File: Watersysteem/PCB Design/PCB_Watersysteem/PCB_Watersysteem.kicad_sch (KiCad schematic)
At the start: 67 parts, among them J1 Height Water, J10 ReferentieProbe, J11 Endstop Lade0, J13 LED Water Level, J14 LED Nutrient Level, J15 Voedingsstoffen 1, J18 Backup GPIO, J19 Voedingsstoffen 2, J2 Height Nutrients, J21 Voedingsstoffen 3, J3 Height Mixer, J4 TestPins, J5 12V ingang, J7 TTL Connector, J8 Endstop UV, J9 Endstop Lade1, SW1 EN, SW2 BOOT, U1 MP1584_Module, U2 ESP32-WROOM-32D, U3 ADS1115IDGS, U4 AMS1117-3.3, U5 MCP23017_SO

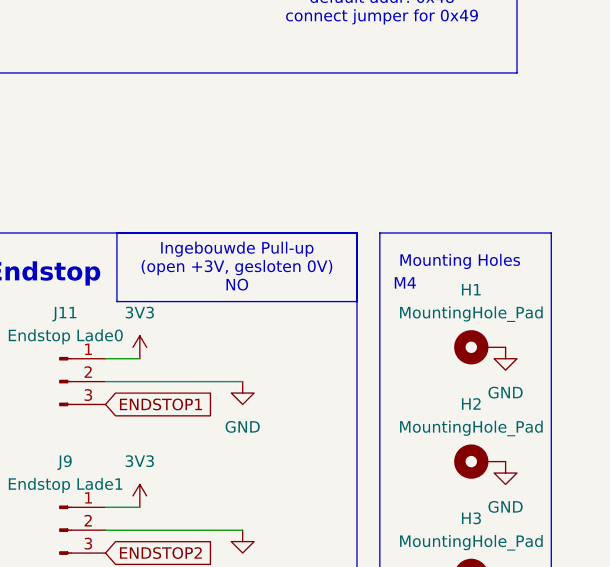
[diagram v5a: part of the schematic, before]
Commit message: Update PCB
M4 -> M3 in Schema
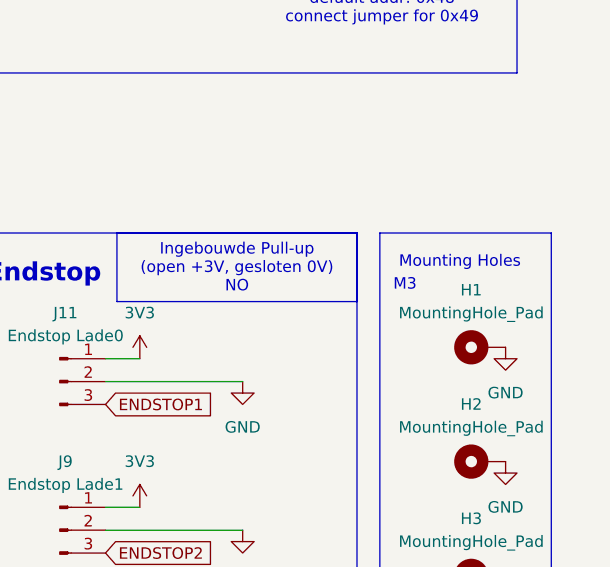
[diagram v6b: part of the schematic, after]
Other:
- note added: "M3"
- note removed: "M4"
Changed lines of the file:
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@@
 		)
 	)
-	(text "M4"
+	(text "M3"
 		(exclude_from_sim no)
 		(at 268.224 112.522 0)

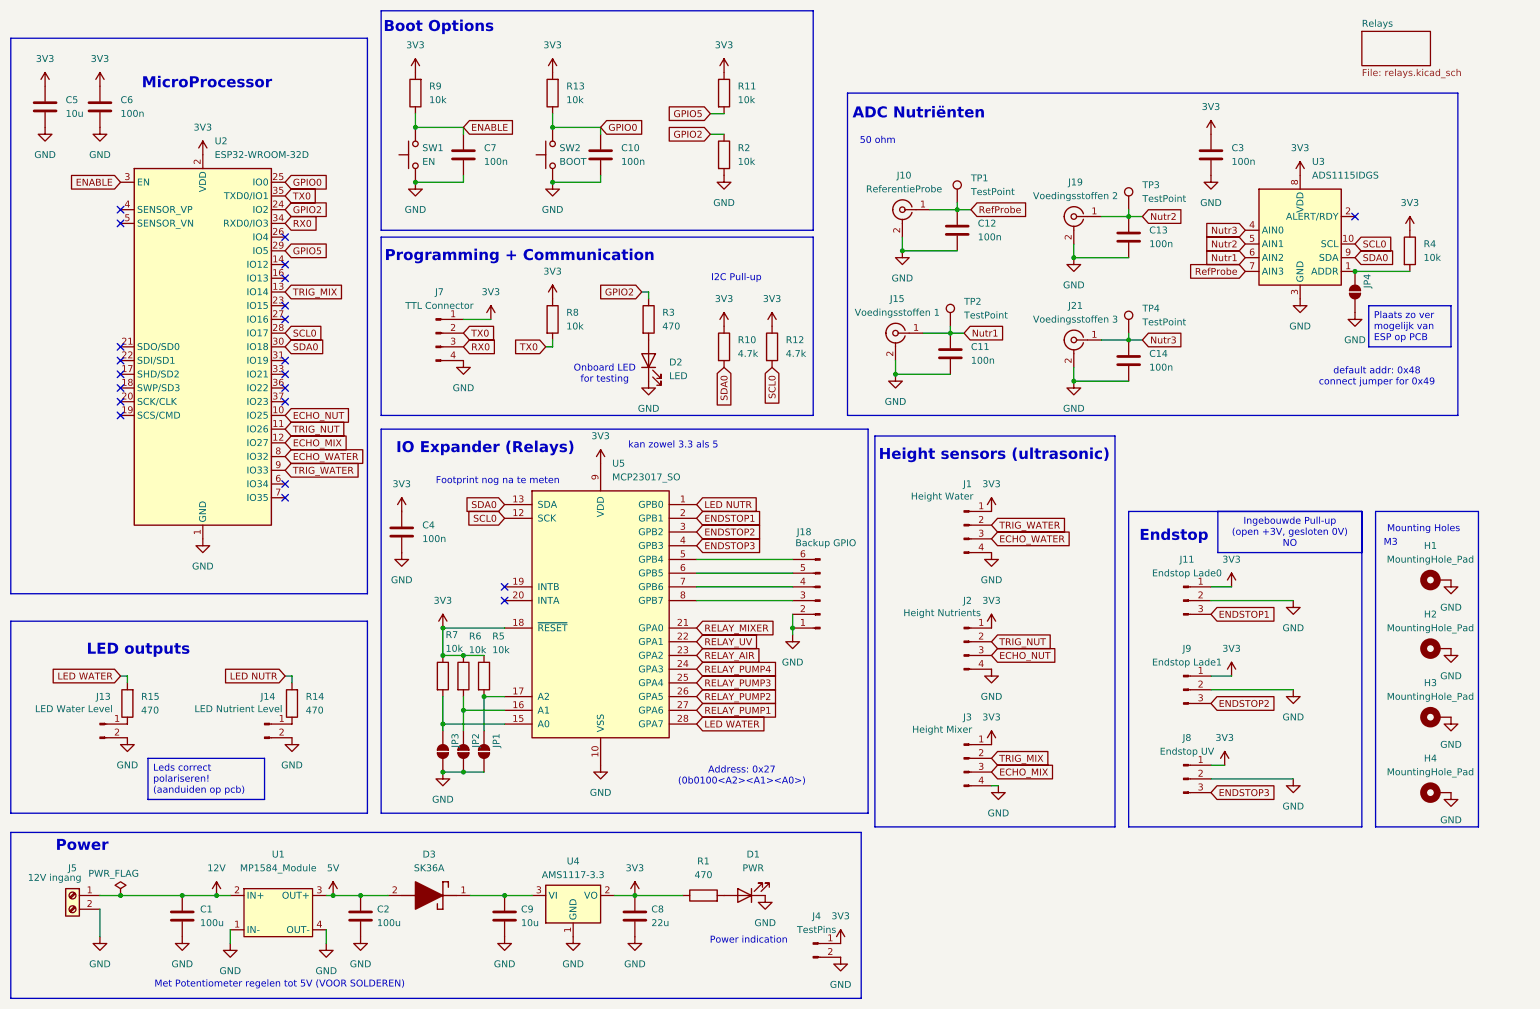
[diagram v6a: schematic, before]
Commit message: Weerstandjes gewijzigd voor status LEDs
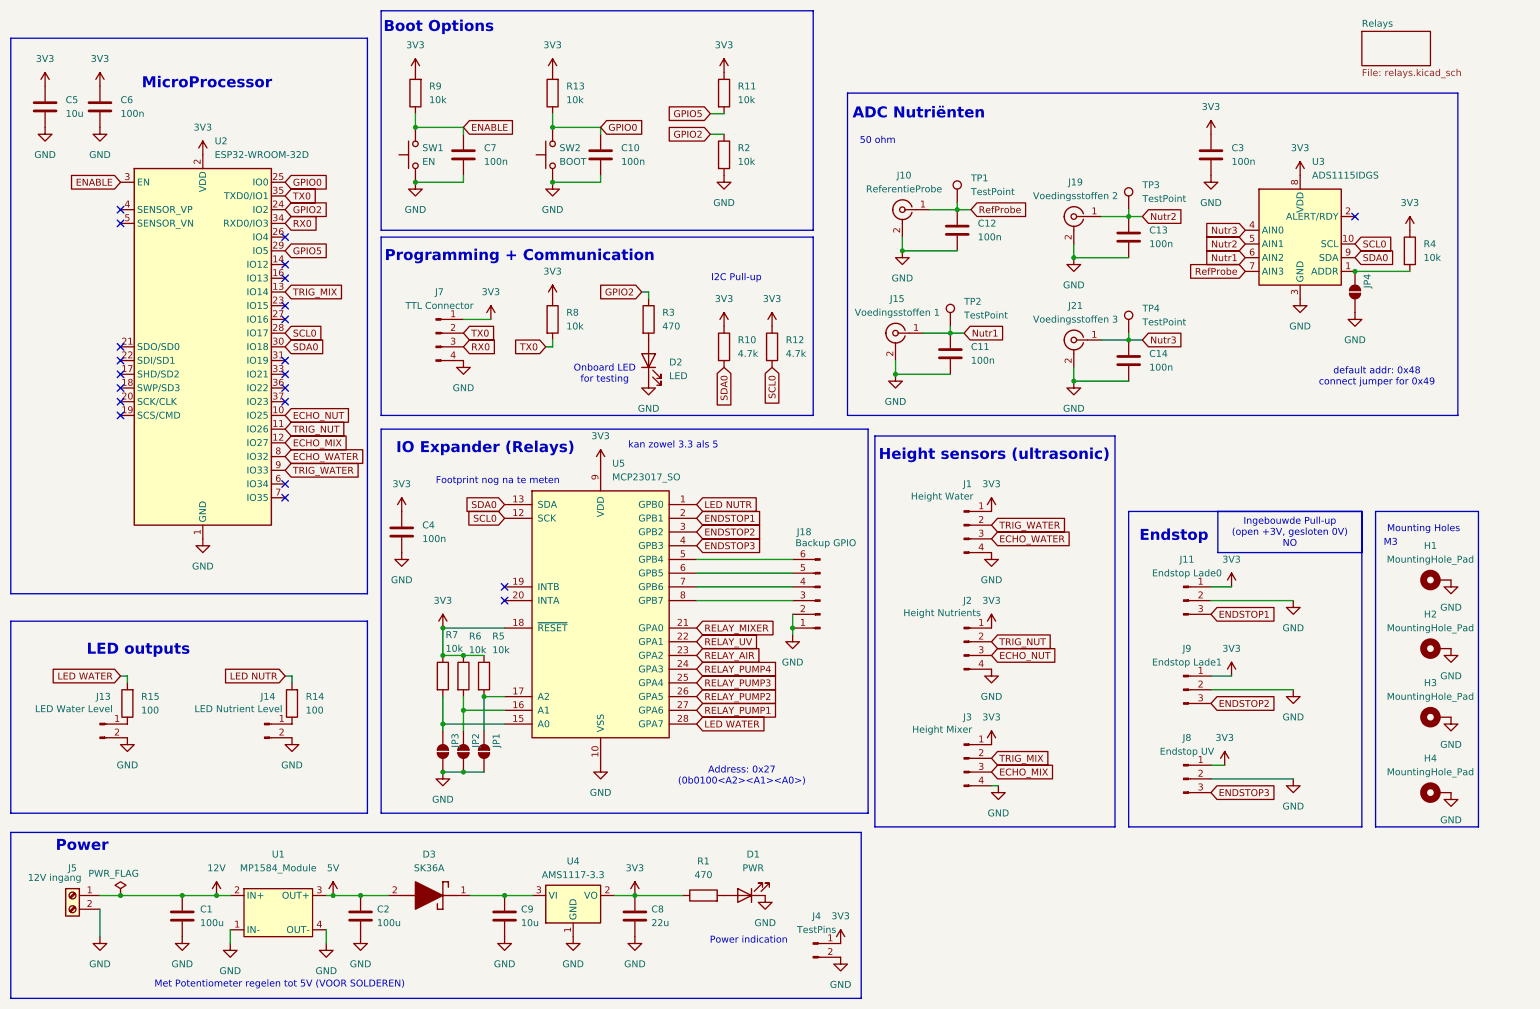
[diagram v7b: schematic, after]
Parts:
- R14, R15: value 470 -> 100
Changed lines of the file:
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@@
 		)
 	)
-	(text_box "Plaats zo ver mogelijk van ESP op PCB"
-		(exclude_from_sim no)
-		(at 264.16 68.58 0)
-		(size 15.24 7.62)
-		(margins 0.9525 0.9525 0.9525 0.9525)
-		(stroke
-			(width 0)
-			(type default)
-		)
-		(fill
-			(type none)
-		)
-		(effects
-			(font
-				(size 1.27 1.27)
-			)
-			(justify left top)
-		)
-	)
-	(text_box "Leds correct polariseren!\n(aanduiden op pcb)"
-		(exclude_from_sim no)
-		(at 38.1 152.4 0)
-		(size 21.59 7.62)
-		(margins 0.9525 0.9525 0.9525 0.9525)
-		(stroke
-			(width 0)
-			(type default)
-		)
-		(fill
-			(type none)
-		)
-		(effects
-			(font
-				(size 1.27 1.27)
-			)
-			(justify left top)
-		)
-	)
 	(junction
 		(at 72.39 177.8)
@@
 			)
 		)
-		(property "Value" "470"
+		(property "Value" "100"
 			(at 67.31 143.5099 0)
 			(effects
@@
 			)
 		)
-		(property "Value" "470"
+		(property "Value" "100"
 			(at 36.83 143.5099 0)
 			(effects
